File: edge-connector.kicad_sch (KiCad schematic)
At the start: 25 parts, among them J9 ocp-dc-scm-spec-rev-1-0-edge-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

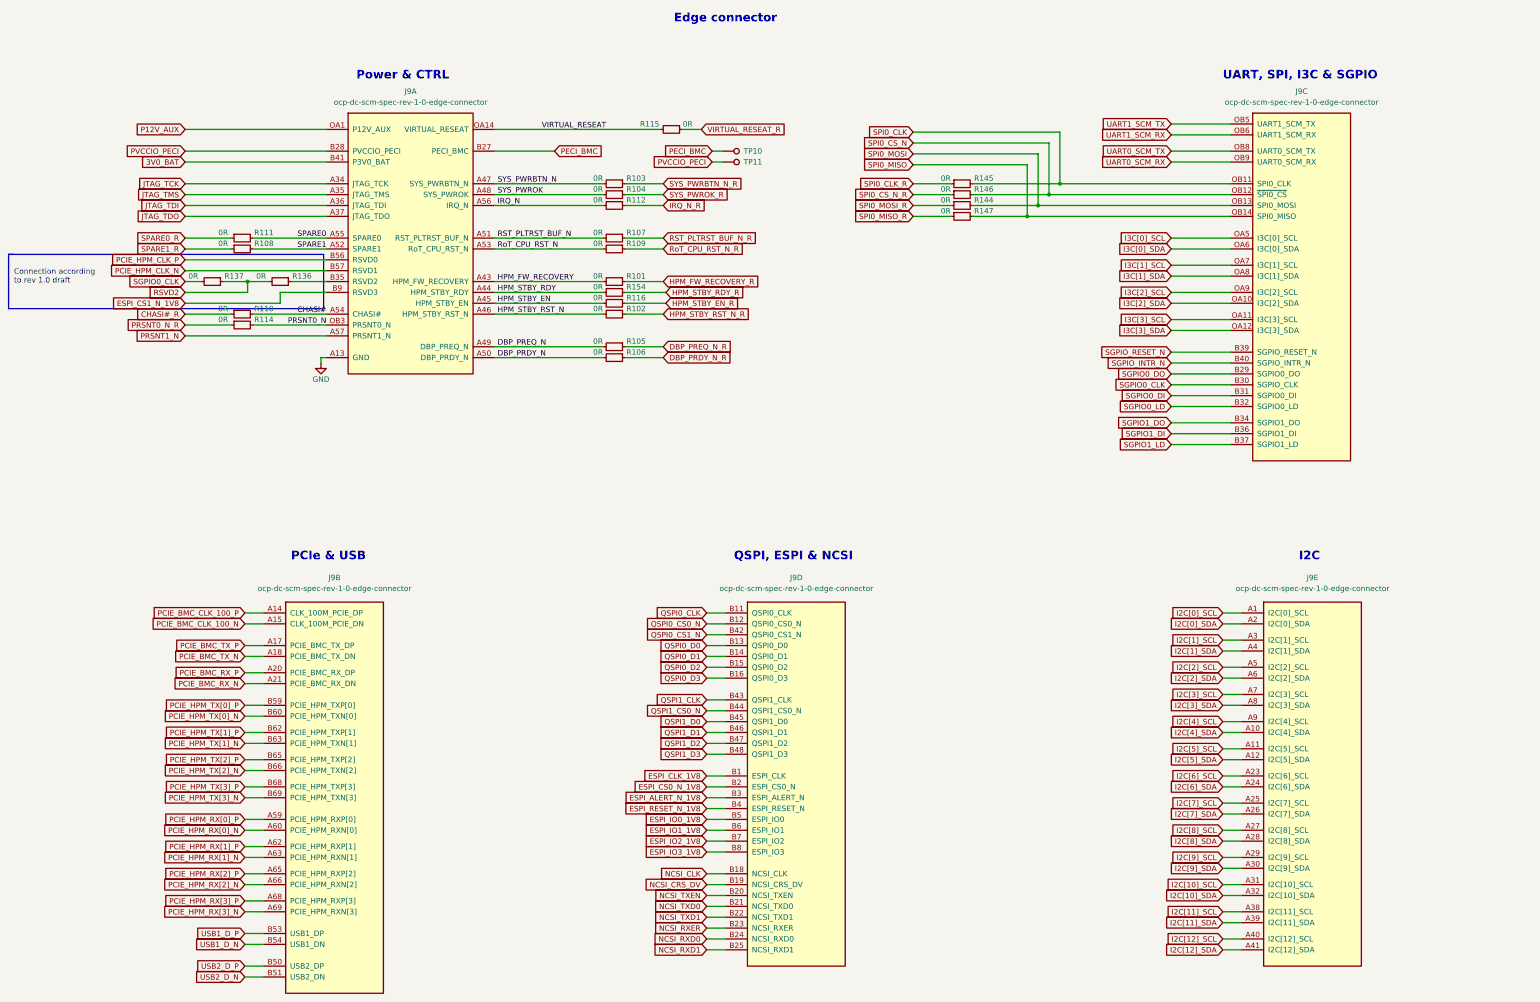
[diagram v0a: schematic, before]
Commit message: [#55652] Fix hotareas
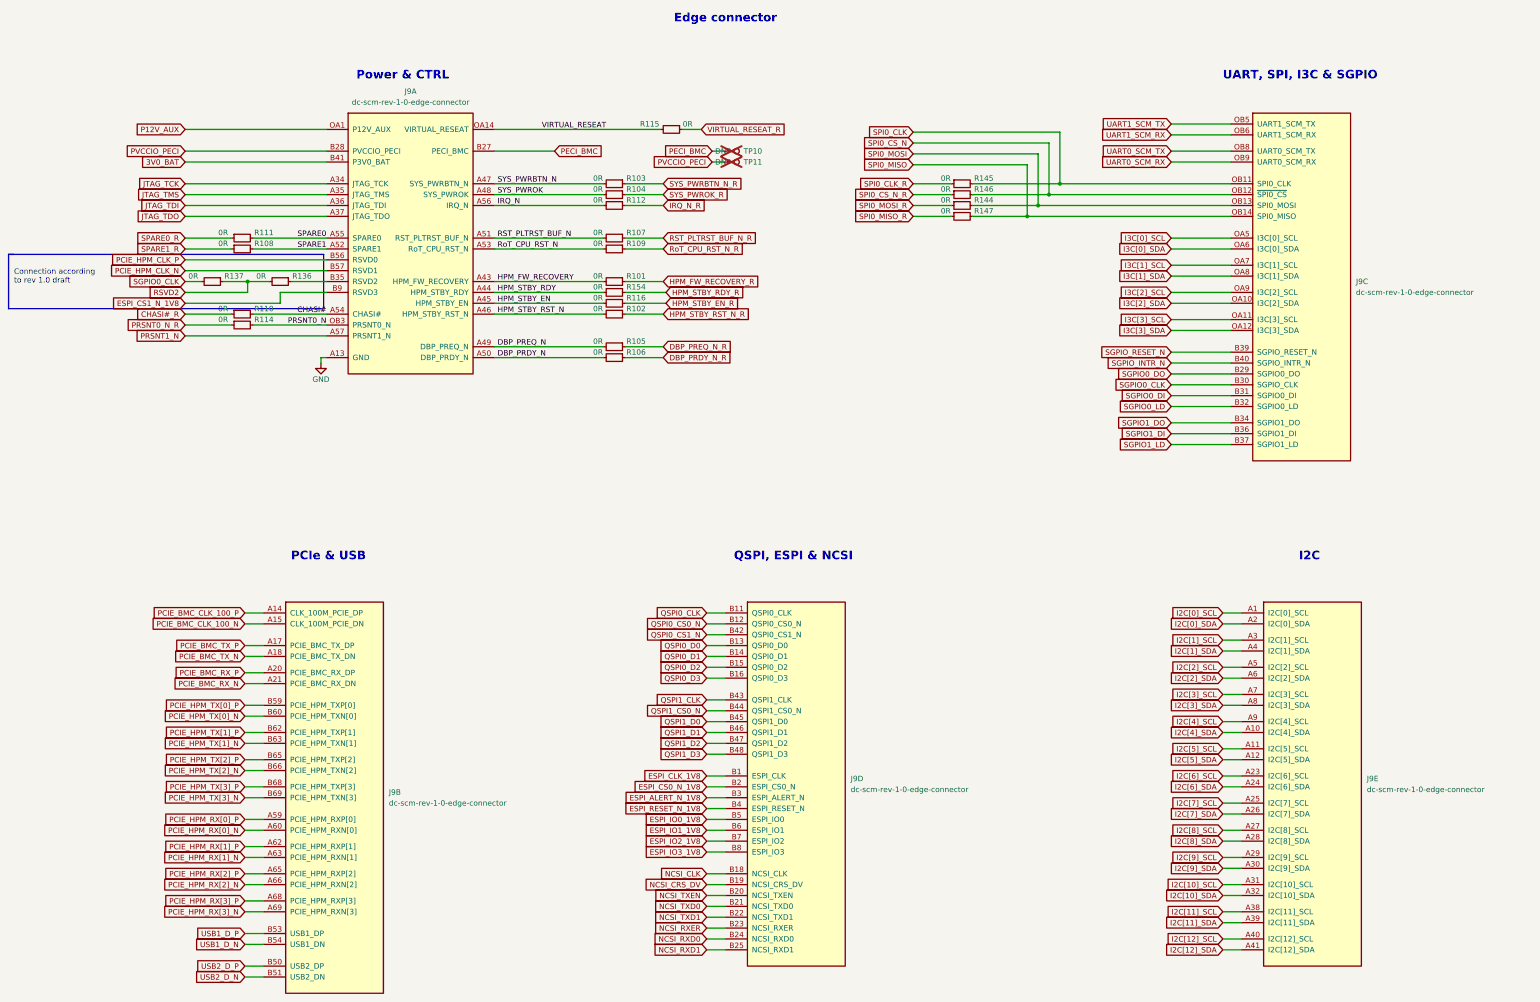
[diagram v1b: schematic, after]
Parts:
- J9: value ocp-dc-scm-spec-rev-1-0-edge-connector -> dc-scm-rev-1-0-edge-connector; footprint antmicro-footprints:SFF-TA-1002-4C+ -> antmicro-footprints:SFF-TA-1002-4C+-rev-1-0-0; symbol antmicroPciConnectors:ocp-dc-scm-spec-rev-1-0-edge-connector -> antmicroPciConnectors:dc-scm-rev-1-0-edge-connector; now left out of the parts list
- TP10, TP11: value TP_SMD1MM -> TP_1mm_SMD; footprint antmicro-footprints:Testpoint_smd_1mm -> antmicro-footprints:TP_SMD_1mm; now not fitted; now left out of the parts list

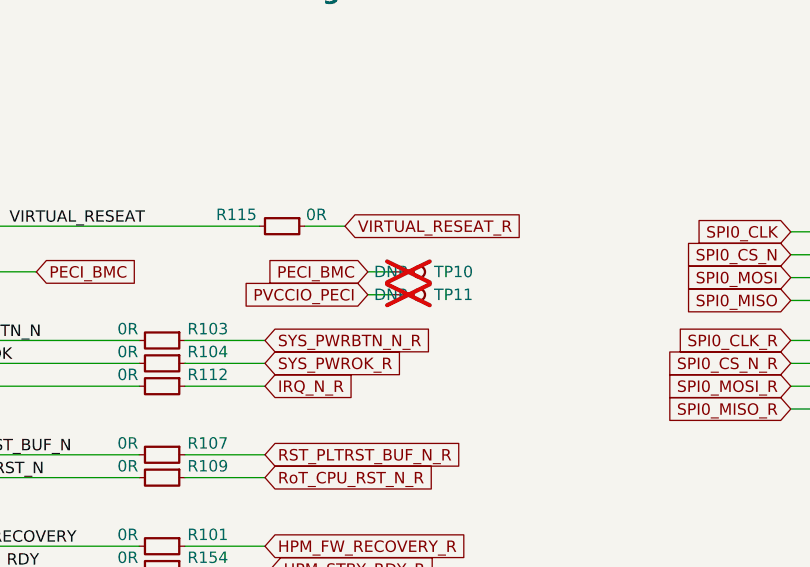
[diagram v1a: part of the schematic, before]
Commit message: [#68236] Update components description
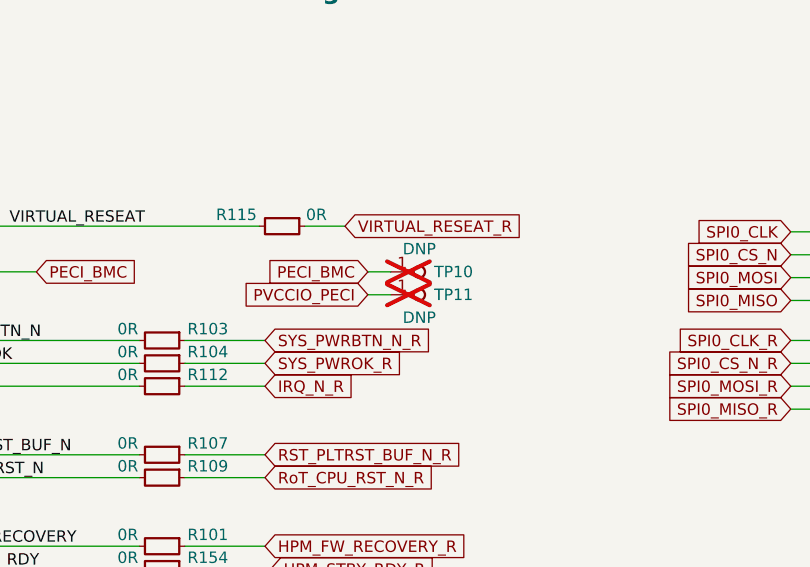
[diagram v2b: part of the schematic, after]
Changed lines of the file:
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@@
       (effects (font (size 1.27 1.27) (thickness 0.15)) (justify left bottom) hide)
     )
-    (property "DNP" "DNP" (at 200.025 53.34 0)
+    (property "DNP" "DNP" (at 203.2 50.8 0)
       (effects (font (size 1.27 1.27)))
     )
@@
     )
   )
-  (symbol (lib_name "TP_1mm_SMD_1") (lib_id "antmicroTestPoints:TP_1mm_SMD") (at 200.025 55.88 0) (mirror x) (unit 1)
+  (symbol (lib_id "antmicroTestPoints:TP_1mm_SMD") (at 200.025 55.88 0) (mirror x) (unit 1)
     (in_bom no) (on_board yes) (dnp yes)
     (property "Reference" "TP11" (at 207.01 55.88 0)
@@
       (effects (font (size 1.27 1.27) (thickness 0.15)) (justify left bottom) hide)
     )
-    (property "DNP" "DNP" (at 200.025 55.88 0)
+    (property "DNP" "DNP" (at 203.2 58.42 0)
       (effects (font (size 1.27 1.27)))
     )
@@
     )
   )
-  (symbol (lib_name "R_0R_0402_1") (lib_id "antmicroResistors0402:R_0R_0402") (at 99.06 83.82 0) (mirror y) (unit 1)
+  (symbol (lib_id "antmicroResistors0402:R_0R_0402") (at 99.06 83.82 0) (mirror y) (unit 1)
     (in_bom yes) (on_board yes) (dnp no)
     (property "Reference" "R136" (at 101.6 82.55 0)
@@
     )
   )
-  (symbol (lib_name "R_0R_0402_7") (lib_id "antmicroResistors0402:R_0R_0402") (at 253.365 60.96 0) (unit 1)
+  (symbol (lib_id "antmicroResistors0402:R_0R_0402") (at 253.365 60.96 0) (unit 1)
     (in_bom yes) (on_board yes) (dnp no)
     (property "Reference" "R145" (at 260.985 59.69 0)
@@
     )
   )
-  (symbol (lib_name "R_0R_0402_23") (lib_id "antmicroResistors0402:R_0R_0402") (at 85.09 76.2 0) (unit 1)
+  (symbol (lib_id "antmicroResistors0402:R_0R_0402") (at 85.09 76.2 0) (unit 1)
     (in_bom yes) (on_board yes) (dnp no) (fields_autoplaced)
     (property "Reference" "R108" (at 92.71 74.93 0)
@@
     )
   )
-  (symbol (lib_name "R_0R_0402_3") (lib_id "antmicroResistors0402:R_0R_0402") (at 177.165 60.96 0) (mirror y) (unit 1)
+  (symbol (lib_id "antmicroResistors0402:R_0R_0402") (at 177.165 60.96 0) (mirror y) (unit 1)
     (in_bom yes) (on_board yes) (dnp no)
     (property "Reference" "R103" (at 179.705 59.69 0)
@@
     )
   )
-  (symbol (lib_name "R_0R_0402_20") (lib_id "antmicroResistors0402:R_0R_0402") (at 177.165 99.06 0) (mirror y) (unit 1)
+  (symbol (lib_id "antmicroResistors0402:R_0R_0402") (at 177.165 99.06 0) (mirror y) (unit 1)
     (in_bom yes) (on_board yes) (dnp no)
     (property "Reference" "R105" (at 179.705 97.79 0)
@@
     )
   )
-  (symbol (lib_name "R_0R_0402_8") (lib_id "antmicroResistors0402:R_0R_0402") (at 253.365 66.04 0) (unit 1)
+  (symbol (lib_id "antmicroResistors0402:R_0R_0402") (at 253.365 66.04 0) (unit 1)
     (in_bom yes) (on_board yes) (dnp no)
     (property "Reference" "R144" (at 260.985 64.77 0)
@@
     )
   )
-  (symbol (lib_name "R_0R_0402_11") (lib_id "antmicroResistors0402:R_0R_0402") (at 85.09 73.66 0) (unit 1)
+  (symbol (lib_id "antmicroResistors0402:R_0R_0402") (at 85.09 73.66 0) (unit 1)
     (in_bom yes) (on_board yes) (dnp no) (fields_autoplaced)
     (property "Reference" "R111" (at 92.71 72.39 0)
@@
     )
   )
-  (symbol (lib_name "R_0R_0402_4") (lib_id "antmicroResistors0402:R_0R_0402") (at 253.365 63.5 0) (unit 1)
+  (symbol (lib_id "antmicroResistors0402:R_0R_0402") (at 253.365 63.5 0) (unit 1)
     (in_bom yes) (on_board yes) (dnp no)
     (property "Reference" "R146" (at 260.985 62.23 0)
@@
     )
   )
-  (symbol (lib_name "R_0R_0402_21") (lib_id "antmicroResistors0402:R_0R_0402") (at 85.09 91.44 0) (unit 1)
+  (symbol (lib_id "antmicroResistors0402:R_0R_0402") (at 85.09 91.44 0) (unit 1)
     (in_bom yes) (on_board yes) (dnp no) (fields_autoplaced)
     (property "Reference" "R110" (at 92.71 90.17 0)
@@
     )
   )
-  (symbol (lib_name "R_0R_0402_13") (lib_id "antmicroResistors0402:R_0R_0402") (at 177.165 101.6 0) (mirror y) (unit 1)
+  (symbol (lib_id "antmicroResistors0402:R_0R_0402") (at 177.165 101.6 0) (mirror y) (unit 1)
     (in_bom yes) (on_board yes) (dnp no)
     (property "Reference" "R106" (at 179.705 100.33 0)
@@
     )
   )
-  (symbol (lib_name "R_0R_0402_12") (lib_id "antmicroResistors0402:R_0R_0402") (at 177.165 76.2 0) (mirror y) (unit 1)
+  (symbol (lib_id "antmicroResistors0402:R_0R_0402") (at 177.165 76.2 0) (mirror y) (unit 1)
     (in_bom yes) (on_board yes) (dnp no)
     (property "Reference" "R109" (at 179.705 74.93 0)
@@
     )
   )
-  (symbol (lib_name "R_0R_0402_24") (lib_id "antmicroResistors0402:R_0R_0402") (at 177.165 86.36 0) (mirror y) (unit 1)
+  (symbol (lib_id "antmicroResistors0402:R_0R_0402") (at 177.165 86.36 0) (mirror y) (unit 1)
     (in_bom yes) (on_board yes) (dnp no)
     (property "Reference" "R154" (at 179.705 85.09 0)
@@
     )
   )
-  (symbol (lib_name "R_0R_0402_15") (lib_id "antmicroResistors0402:R_0R_0402") (at 177.165 73.66 0) (mirror y) (unit 1)
+  (symbol (lib_id "antmicroResistors0402:R_0R_0402") (at 177.165 73.66 0) (mirror y) (unit 1)
     (in_bom yes) (on_board yes) (dnp no)
     (property "Reference" "R107" (at 179.705 72.39 0)
@@
     )
   )
-  (symbol (lib_name "R_0R_0402_22") (lib_id "antmicroResistors0402:R_0R_0402") (at 177.165 66.04 0) (mirror y) (unit 1)
+  (symbol (lib_id "antmicroResistors0402:R_0R_0402") (at 177.165 66.04 0) (mirror y) (unit 1)
     (in_bom yes) (on_board yes) (dnp no)
     (property "Reference" "R112" (at 179.705 64.77 0)
@@
     )
   )
-  (symbol (lib_name "R_0R_0402_14") (lib_id "antmicroResistors0402:R_0R_0402") (at 177.165 63.5 0) (mirror y) (unit 1)
+  (symbol (lib_id "antmicroResistors0402:R_0R_0402") (at 177.165 63.5 0) (mirror y) (unit 1)
     (in_bom yes) (on_board yes) (dnp no)
     (property "Reference" "R104" (at 179.705 62.23 0)
@@
     )
   )
-  (symbol (lib_name "R_0R_0402_10") (lib_id "antmicroResistors0402:R_0R_0402") (at 190.5 48.26 0) (mirror y) (unit 1)
+  (symbol (lib_id "antmicroResistors0402:R_0R_0402") (at 190.5 48.26 0) (mirror y) (unit 1)
     (in_bom yes) (on_board yes) (dnp no)
     (property "Reference" "R115" (at 182.88 46.99 0)
@@
     )
   )
-  (symbol (lib_name "R_0R_0402_5") (lib_id "antmicroResistors0402:R_0R_0402") (at 253.365 68.58 0) (unit 1)
+  (symbol (lib_id "antmicroResistors0402:R_0R_0402") (at 253.365 68.58 0) (unit 1)
     (in_bom yes) (on_board yes) (dnp no)
     (property "Reference" "R147" (at 260.985 67.31 0)
@@
     )
   )
-  (symbol (lib_name "R_0R_0402_6") (lib_id "antmicroResistors0402:R_0R_0402") (at 177.165 83.82 0) (mirror y) (unit 1)
+  (symbol (lib_id "antmicroResistors0402:R_0R_0402") (at 177.165 83.82 0) (mirror y) (unit 1)
     (in_bom yes) (on_board yes) (dnp no)
     (property "Reference" "R101" (at 179.705 82.55 0)
@@
     )
   )
-  (symbol (lib_name "R_0R_0402_9") (lib_id "antmicroResistors0402:R_0R_0402") (at 85.09 93.98 0) (unit 1)
+  (symbol (lib_id "antmicroResistors0402:R_0R_0402") (at 85.09 93.98 0) (unit 1)
     (in_bom yes) (on_board yes) (dnp no)
     (property "Reference" "R114" (at 92.71 92.71 0)
@@
     )
   )
-  (symbol (lib_name "R_0R_0402_2") (lib_id "antmicroResistors0402:R_0R_0402") (at 177.165 91.44 0) (mirror y) (unit 1)
+  (symbol (lib_id "antmicroResistors0402:R_0R_0402") (at 177.165 91.44 0) (mirror y) (unit 1)
     (in_bom yes) (on_board yes) (dnp no)
     (property "Reference" "R102" (at 179.705 90.17 0)

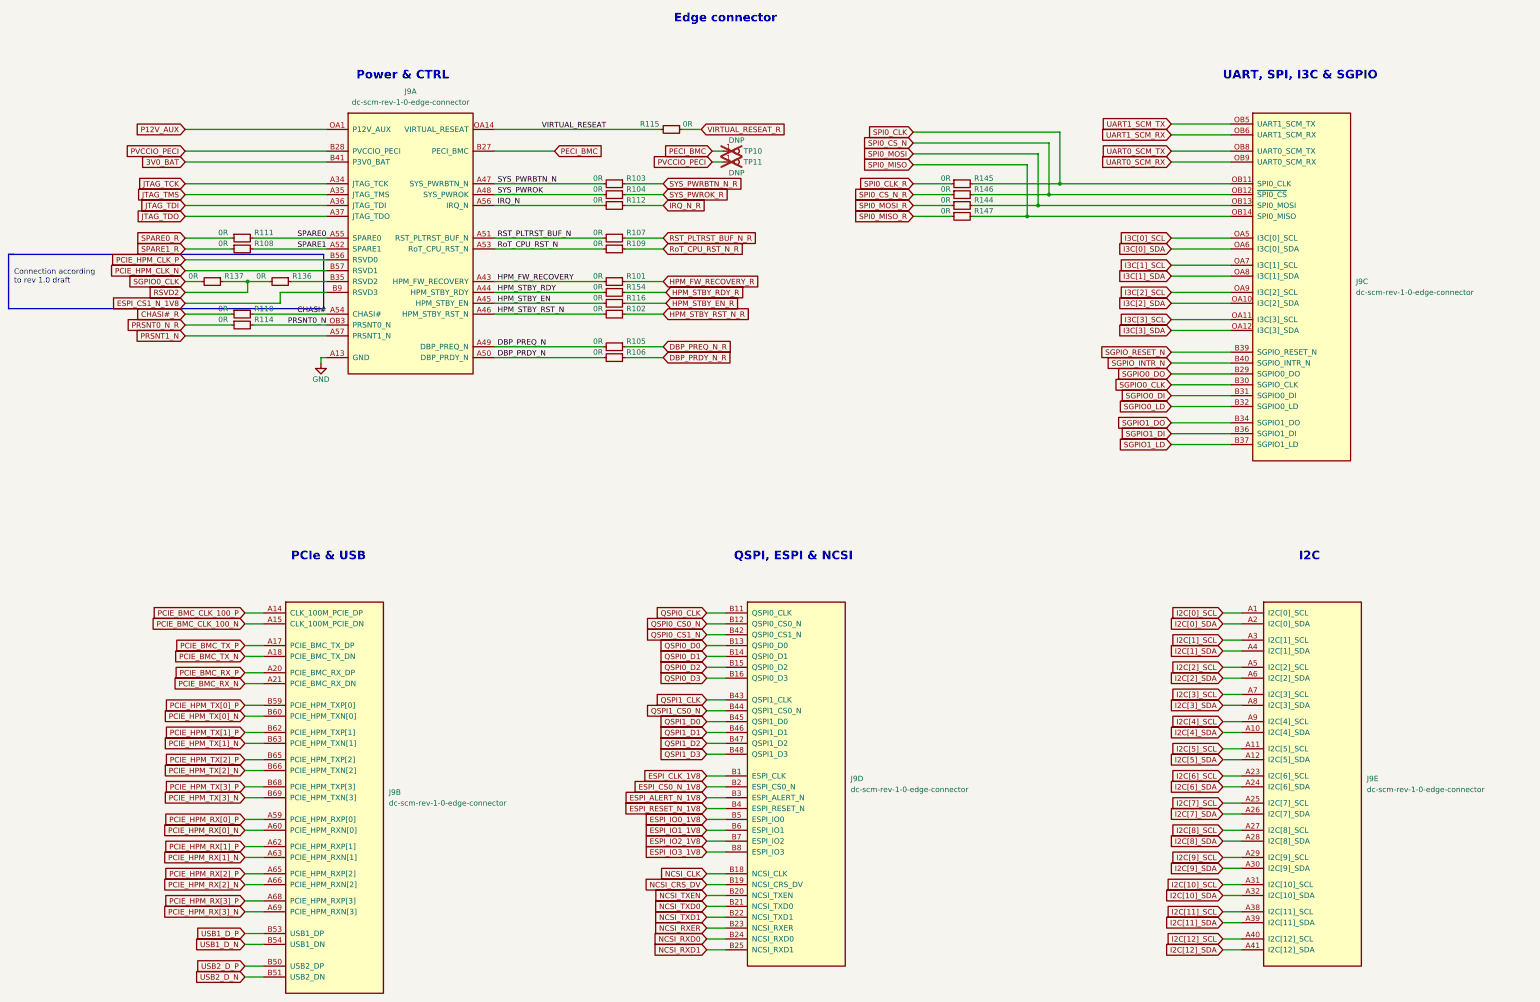
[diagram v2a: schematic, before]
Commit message: [#68236] Allign sch to grid
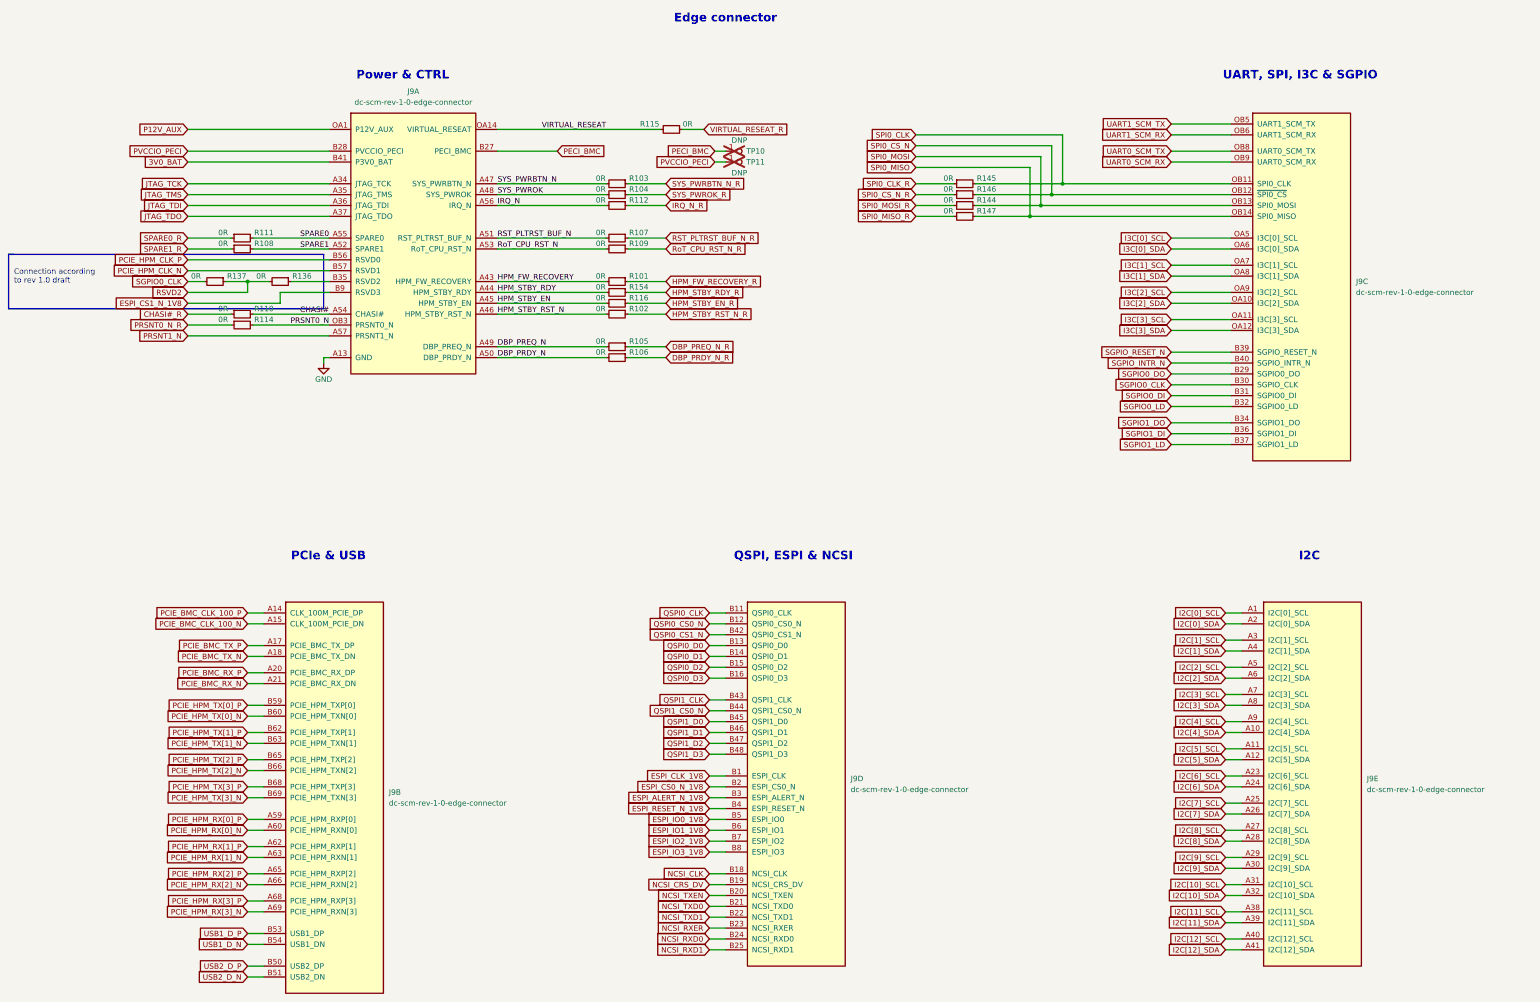
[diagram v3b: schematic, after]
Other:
- moved on the sheet: J9A, R101, R102, R103, R104, R105, R106, R107, R109, R112, R116, R137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
